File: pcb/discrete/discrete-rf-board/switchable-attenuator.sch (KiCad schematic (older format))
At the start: 11 parts, among them U1101 BGS12PL6E6327XTSA1, U1102 BGS12PL6E6327XTSA1

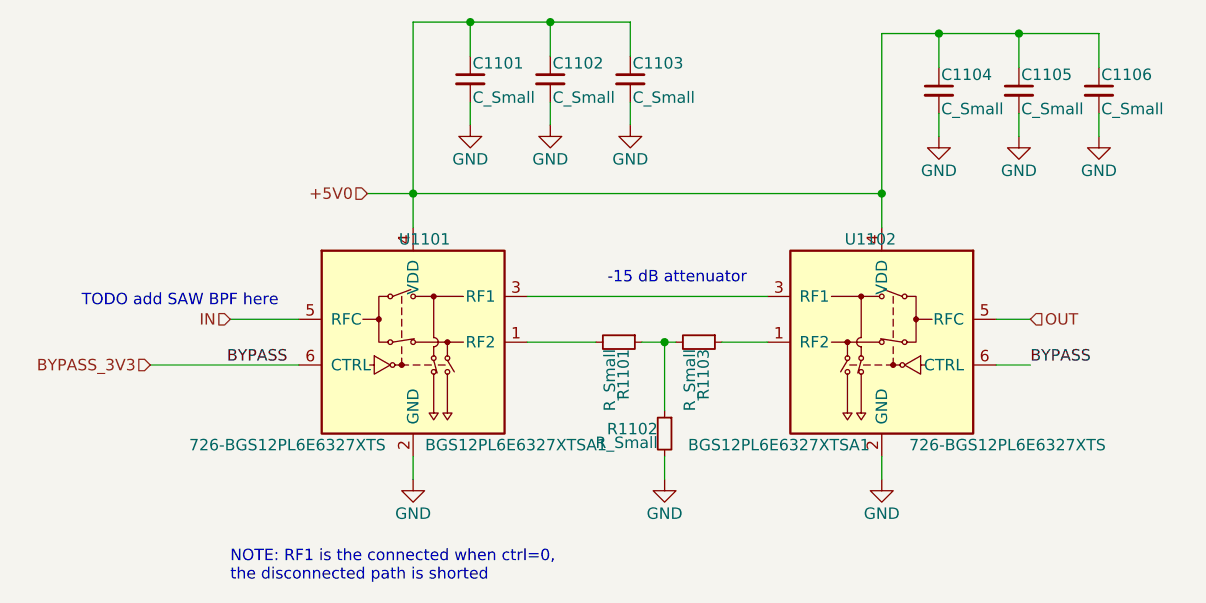
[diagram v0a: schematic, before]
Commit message: Wire out all control signals to connectors TODO PLL charge pump loop, bypass caps in attenuator circuit, antialiasing filter for ADC frontend
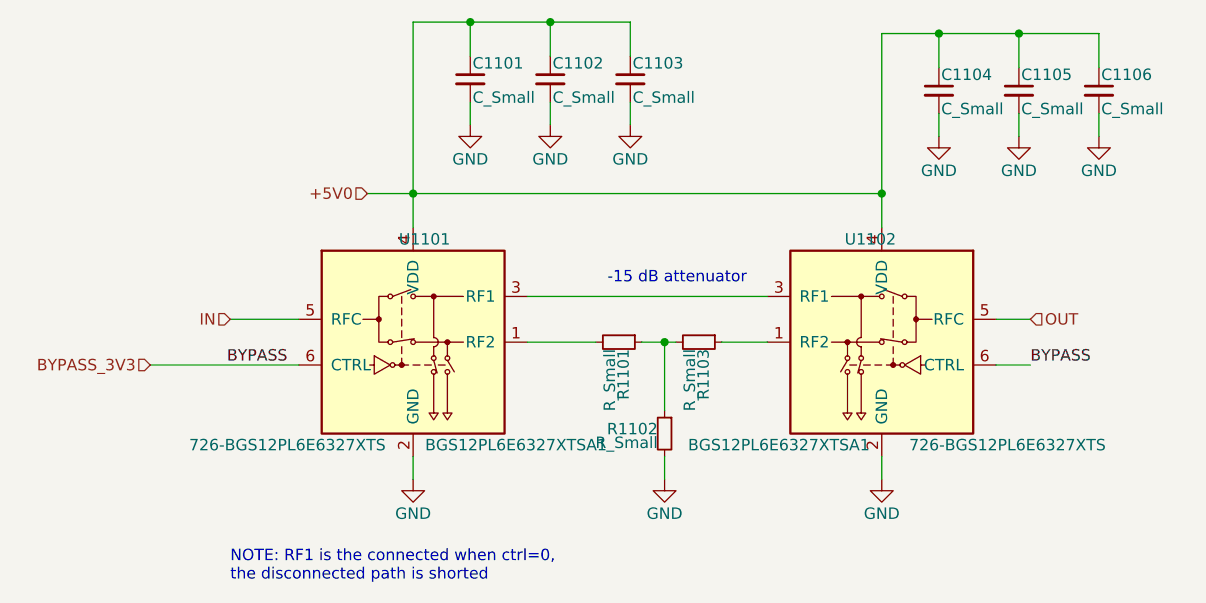
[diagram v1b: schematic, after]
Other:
- note removed: "TODO add SAW BPF here"
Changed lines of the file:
@@
 $Descr A4 11693 8268
 encoding utf-8
-Sheet 11 19
+Sheet 17 19
 Title ""
 Date ""
@@
 	1    0    0    -1
 $EndComp
-Text Notes 2500 3150 0    50   ~ 0
-TODO add SAW BPF here
 $Comp
 L Device:R_Small R?

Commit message: Start work in footprinting everything
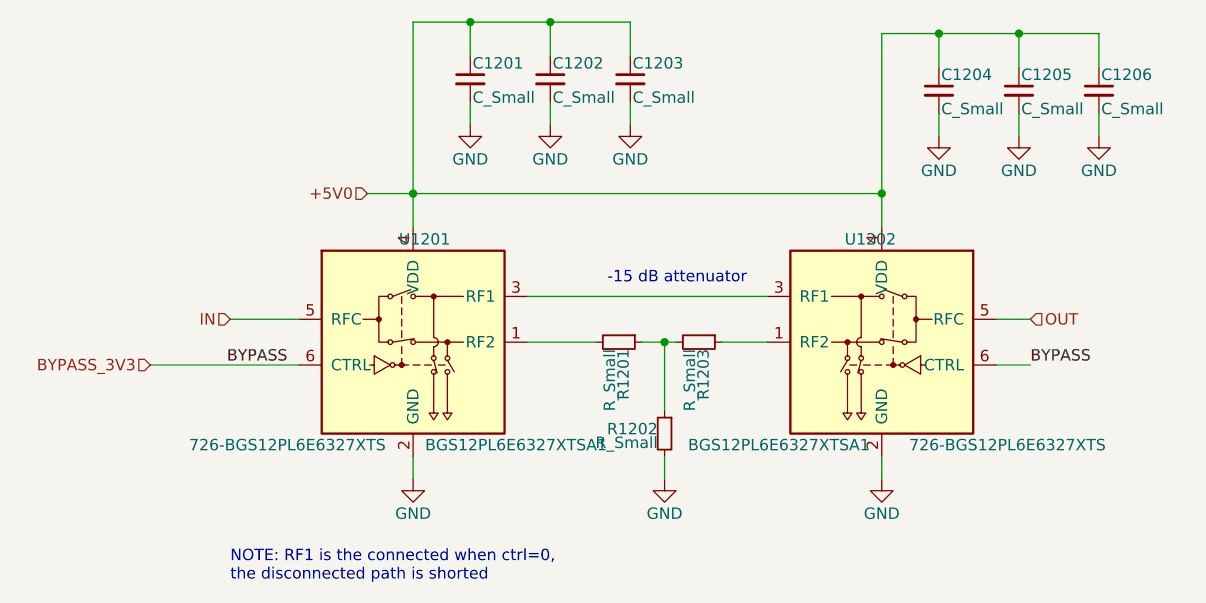
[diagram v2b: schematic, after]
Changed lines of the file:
@@
 $Descr A4 11693 8268
 encoding utf-8
-Sheet 17 19
+Sheet 18 19
 Title ""
 Date ""
@@
 AR Path="/5CA6B0AA/5CE74EBE/5D4B0AA8/5D4B1FC3" Ref="U1101"  Part="1"
 AR Path="/5CA6B0AA/5CE74EBE/5D4C7749/5D4B1FC3" Ref="U1201"  Part="1"
-F 0 "U1101" H 4000 3750 50  0000 C CNN
+F 0 "U1201" H 4000 3750 50  0000 C CNN
 F 1 "BGS12PL6E6327XTSA1" H 4400 2850 50  0000 C CNN
 F 2 "" H 3950 3300 50  0001 C CNN
@@
 AR Path="/5CA6B0AA/5CE74EBE/5D4B0AA8/5D4B1FCA" Ref="R1101"  Part="1"
 AR Path="/5CA6B0AA/5CE74EBE/5D4C7749/5D4B1FCA" Ref="R1201"  Part="1"
-F 0 "R1101" H 4880 3320 50  0000 L CNN
+F 0 "R1201" H 4880 3320 50  0000 L CNN
 F 1 "R_Small" H 4880 3260 50  0000 L CNN
 F 2 "" H 4850 3300 50  0001 C CNN
@@
 AR Path="/5CA6B0AA/5CE74EBE/5D4B0AA8/5D4B1FD0" Ref="R1103"  Part="1"
 AR Path="/5CA6B0AA/5CE74EBE/5D4C7749/5D4B1FD0" Ref="R1203"  Part="1"
-F 0 "R1103" H 5230 3320 50  0000 L CNN
+F 0 "R1203" H 5230 3320 50  0000 L CNN
 F 1 "R_Small" H 5230 3260 50  0000 L CNN
 F 2 "" H 5200 3300 50  0001 C CNN
@@
 AR Path="/5CA6B0AA/5CE74EBE/5D4B0AA8/5D4B1FD6" Ref="R1102"  Part="1"
 AR Path="/5CA6B0AA/5CE74EBE/5D4C7749/5D4B1FD6" Ref="R1202"  Part="1"
-F 0 "R1102" H 5080 3720 50  0000 L CNN
+F 0 "R1202" H 5080 3720 50  0000 L CNN
 F 1 "R_Small" H 5080 3660 50  0000 L CNN
 F 2 "" H 5050 3700 50  0001 C CNN
@@
 AR Path="/5CA6B0AA/5CE74EBE/5D4B0AA8/5D4B1FDD" Ref="#PWR01101"  Part="1"
 AR Path="/5CA6B0AA/5CE74EBE/5D4C7749/5D4B1FDD" Ref="#PWR01201"  Part="1"
-F 0 "#PWR01101" H 3950 3650 50  0001 C CNN
+F 0 "#PWR01201" H 3950 3650 50  0001 C CNN
 F 1 "GND" H 3950 3750 50  0000 C CNN
 F 2 "" H 3950 3900 50  0001 C CNN
@@
 AR Path="/5CA6B0AA/5CE74EBE/5D4B0AA8/5D4B1FE5" Ref="#PWR01105"  Part="1"
 AR Path="/5CA6B0AA/5CE74EBE/5D4C7749/5D4B1FE5" Ref="#PWR01205"  Part="1"
-F 0 "#PWR01105" H 5050 3650 50  0001 C CNN
+F 0 "#PWR01205" H 5050 3650 50  0001 C CNN
 F 1 "GND" H 5050 3750 50  0000 C CNN
 F 2 "" H 5050 3900 50  0001 C CNN
@@
 AR Path="/5CA6B0AA/5CE74EBE/5D4B0AA8/5D4B2001" Ref="#PWR01106"  Part="1"
 AR Path="/5CA6B0AA/5CE74EBE/5D4C7749/5D4B2001" Ref="#PWR01206"  Part="1"
-F 0 "#PWR01106" H 6000 3650 50  0001 C CNN
+F 0 "#PWR01206" H 6000 3650 50  0001 C CNN
 F 1 "GND" H 6000 3750 50  0000 C CNN
 F 2 "" H 6000 3900 50  0001 C CNN
@@
 AR Path="/5CA6B0AA/5CE74EBE/5D4B0AA8/5D4B1FF8" Ref="U1102"  Part="1"
 AR Path="/5CA6B0AA/5CE74EBE/5D4C7749/5D4B1FF8" Ref="U1202"  Part="1"
-F 0 "U1102" H 6050 3750 50  0000 C CNN
+F 0 "U1202" H 6050 3750 50  0000 C CNN
 F 1 "BGS12PL6E6327XTSA1" H 6450 2850 50  0000 C CNN
 F 2 "" H 6000 3300 50  0001 C CNN
@@
 AR Path="/5CA6B0AA/5CE74EBE/5D4B0AA8/5D4BC42E" Ref="C1101"  Part="1"
 AR Path="/5CA6B0AA/5CE74EBE/5D4C7749/5D4BC42E" Ref="C1201"  Part="1"
-F 0 "C1101" H 4210 2220 50  0000 L CNN
+F 0 "C1201" H 4210 2220 50  0000 L CNN
 F 1 "C_Small" H 4210 2070 50  0000 L CNN
 F 2 "" H 4200 2150 50  0001 C CNN
@@
 AR Path="/5CA6B0AA/5CE74EBE/5D4B0AA8/5D4BC853" Ref="C1102"  Part="1"
 AR Path="/5CA6B0AA/5CE74EBE/5D4C7749/5D4BC853" Ref="C1202"  Part="1"
-F 0 "C1102" H 4560 2220 50  0000 L CNN
+F 0 "C1202" H 4560 2220 50  0000 L CNN
 F 1 "C_Small" H 4560 2070 50  0000 L CNN
 F 2 "" H 4550 2150 50  0001 C CNN
@@
 AR Path="/5CA6B0AA/5CE74EBE/5D4B0AA8/5D4BCC70" Ref="C1103"  Part="1"
 AR Path="/5CA6B0AA/5CE74EBE/5D4C7749/5D4BCC70" Ref="C1203"  Part="1"
-F 0 "C1103" H 4910 2220 50  0000 L CNN
+F 0 "C1203" H 4910 2220 50  0000 L CNN
 F 1 "C_Small" H 4910 2070 50  0000 L CNN
 F 2 "" H 4900 2150 50  0001 C CNN
@@
 AR Path="/5CA6B0AA/5CE74EBE/5D4B0AA8/5D4BED00" Ref="C1104"  Part="1"
 AR Path="/5CA6B0AA/5CE74EBE/5D4C7749/5D4BED00" Ref="C1204"  Part="1"
-F 0 "C1104" H 6260 2270 50  0000 L CNN
+F 0 "C1204" H 6260 2270 50  0000 L CNN
 F 1 "C_Small" H 6260 2120 50  0000 L CNN
 F 2 "" H 6250 2200 50  0001 C CNN
@@
 AR Path="/5CA6B0AA/5CE74EBE/5D4B0AA8/5D4BED06" Ref="C1105"  Part="1"
 AR Path="/5CA6B0AA/5CE74EBE/5D4C7749/5D4BED06" Ref="C1205"  Part="1"
-F 0 "C1105" H 6610 2270 50  0000 L CNN
+F 0 "C1205" H 6610 2270 50  0000 L CNN
 F 1 "C_Small" H 6610 2120 50  0000 L CNN
 F 2 "" H 6600 2200 50  0001 C CNN
@@
 AR Path="/5CA6B0AA/5CE74EBE/5D4B0AA8/5D4BED0C" Ref="C1106"  Part="1"
 AR Path="/5CA6B0AA/5CE74EBE/5D4C7749/5D4BED0C" Ref="C1206"  Part="1"
-F 0 "C1106" H 6960 2270 50  0000 L CNN
+F 0 "C1206" H 6960 2270 50  0000 L CNN
 F 1 "C_Small" H 6960 2120 50  0000 L CNN
 F 2 "" H 6950 2200 50  0001 C CNN
@@
 AR Path="/5CA6B0AA/5CE74EBE/5D4B0AA8/5D4BF277" Ref="#PWR01109"  Part="1"
 AR Path="/5CA6B0AA/5CE74EBE/5D4C7749/5D4BF277" Ref="#PWR01209"  Part="1"
-F 0 "#PWR01109" H 6950 2150 50  0001 C CNN
+F 0 "#PWR01209" H 6950 2150 50  0001 C CNN
 F 1 "GND" H 6950 2250 50  0000 C CNN
 F 2 "" H 6950 2400 50  0001 C CNN
@@
 AR Path="/5CA6B0AA/5CE74EBE/5D4B0AA8/5D4BF7E8" Ref="#PWR01108"  Part="1"
 AR Path="/5CA6B0AA/5CE74EBE/5D4C7749/5D4BF7E8" Ref="#PWR01208"  Part="1"
-F 0 "#PWR01108" H 6600 2150 50  0001 C CNN
+F 0 "#PWR01208" H 6600 2150 50  0001 C CNN
 F 1 "GND" H 6600 2250 50  0000 C CNN
 F 2 "" H 6600 2400 50  0001 C CNN
@@
 AR Path="/5CA6B0AA/5CE74EBE/5D4B0AA8/5D4BFA67" Ref="#PWR01107"  Part="1"
 AR Path="/5CA6B0AA/5CE74EBE/5D4C7749/5D4BFA67" Ref="#PWR01207"  Part="1"
-F 0 "#PWR01107" H 6250 2150 50  0001 C CNN
+F 0 "#PWR01207" H 6250 2150 50  0001 C CNN
 F 1 "GND" H 6250 2250 50  0000 C CNN
 F 2 "" H 6250 2400 50  0001 C CNN
@@
 AR Path="/5CA6B0AA/5CE74EBE/5D4B0AA8/5D4C425B" Ref="#PWR01104"  Part="1"
 AR Path="/5CA6B0AA/5CE74EBE/5D4C7749/5D4C425B" Ref="#PWR01204"  Part="1"
-F 0 "#PWR01104" H 4900 2100 50  0001 C CNN
+F 0 "#PWR01204" H 4900 2100 50  0001 C CNN
 F 1 "GND" H 4900 2200 50  0000 C CNN
 F 2 "" H 4900 2350 50  0001 C CNN
@@
 AR Path="/5CA6B0AA/5CE74EBE/5D4B0AA8/5D4C4261" Ref="#PWR01103"  Part="1"
 AR Path="/5CA6B0AA/5CE74EBE/5D4C7749/5D4C4261" Ref="#PWR01203"  Part="1"
-F 0 "#PWR01103" H 4550 2100 50  0001 C CNN
+F 0 "#PWR01203" H 4550 2100 50  0001 C CNN
 F 1 "GND" H 4550 2200 50  0000 C CNN
 F 2 "" H 4550 2350 50  0001 C CNN
@@
 AR Path="/5CA6B0AA/5CE74EBE/5D4B0AA8/5D4C4267" Ref="#PWR01102"  Part="1"
 AR Path="/5CA6B0AA/5CE74EBE/5D4C7749/5D4C4267" Ref="#PWR01202"  Part="1"
-F 0 "#PWR01102" H 4200 2100 50  0001 C CNN
+F 0 "#PWR01202" H 4200 2100 50  0001 C CNN
 F 1 "GND" H 4200 2200 50  0000 C CNN
 F 2 "" H 4200 2350 50  0001 C CNN

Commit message: Fix some parts
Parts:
- U1101: footprint (none) -> discrete_footprints:Infineon_TSLP-6-4
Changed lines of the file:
@@
 $Descr A4 11693 8268
 encoding utf-8
-Sheet 18 19
+Sheet 17 19
 Title ""
 Date ""
@@
 AR Path="/5CA6B0AA/5CE74EBE/5D4B0AA8/5D4B1FC3" Ref="U1101"  Part="1"
 AR Path="/5CA6B0AA/5CE74EBE/5D4C7749/5D4B1FC3" Ref="U1201"  Part="1"
-F 0 "U1201" H 4000 3750 50  0000 C CNN
+F 0 "U1101" H 4000 3750 50  0000 C CNN
 F 1 "BGS12PL6E6327XTSA1" H 4400 2850 50  0000 C CNN
-F 2 "" H 3950 3300 50  0001 C CNN
+F 2 "discrete_footprints:Infineon_TSLP-6-4" H 3950 3300 50  0001 C CNN
 F 3 "" H 3950 3300 50  0001 C CNN
 F 4 "726-BGS12PL6E6327XTS" H 3400 2850 50  0000 C CNN "Mouser"
@@
 AR Path="/5CA6B0AA/5CE74EBE/5D4B0AA8/5D4B1FCA" Ref="R1101"  Part="1"
 AR Path="/5CA6B0AA/5CE74EBE/5D4C7749/5D4B1FCA" Ref="R1201"  Part="1"
-F 0 "R1201" H 4880 3320 50  0000 L CNN
+F 0 "R1101" H 4880 3320 50  0000 L CNN
 F 1 "R_Small" H 4880 3260 50  0000 L CNN
 F 2 "" H 4850 3300 50  0001 C CNN
@@
 AR Path="/5CA6B0AA/5CE74EBE/5D4B0AA8/5D4B1FD0" Ref="R1103"  Part="1"
 AR Path="/5CA6B0AA/5CE74EBE/5D4C7749/5D4B1FD0" Ref="R1203"  Part="1"
-F 0 "R1203" H 5230 3320 50  0000 L CNN
+F 0 "R1103" H 5230 3320 50  0000 L CNN
 F 1 "R_Small" H 5230 3260 50  0000 L CNN
 F 2 "" H 5200 3300 50  0001 C CNN
@@
 AR Path="/5CA6B0AA/5CE74EBE/5D4B0AA8/5D4B1FD6" Ref="R1102"  Part="1"
 AR Path="/5CA6B0AA/5CE74EBE/5D4C7749/5D4B1FD6" Ref="R1202"  Part="1"
-F 0 "R1202" H 5080 3720 50  0000 L CNN
+F 0 "R1102" H 5080 3720 50  0000 L CNN
 F 1 "R_Small" H 5080 3660 50  0000 L CNN
 F 2 "" H 5050 3700 50  0001 C CNN
@@
 AR Path="/5CA6B0AA/5CE74EBE/5D4B0AA8/5D4B1FDD" Ref="#PWR01101"  Part="1"
 AR Path="/5CA6B0AA/5CE74EBE/5D4C7749/5D4B1FDD" Ref="#PWR01201"  Part="1"
-F 0 "#PWR01201" H 3950 3650 50  0001 C CNN
+F 0 "#PWR01101" H 3950 3650 50  0001 C CNN
 F 1 "GND" H 3950 3750 50  0000 C CNN
 F 2 "" H 3950 3900 50  0001 C CNN
@@
 AR Path="/5CA6B0AA/5CE74EBE/5D4B0AA8/5D4B1FE5" Ref="#PWR01105"  Part="1"
 AR Path="/5CA6B0AA/5CE74EBE/5D4C7749/5D4B1FE5" Ref="#PWR01205"  Part="1"
-F 0 "#PWR01205" H 5050 3650 50  0001 C CNN
+F 0 "#PWR01105" H 5050 3650 50  0001 C CNN
 F 1 "GND" H 5050 3750 50  0000 C CNN
 F 2 "" H 5050 3900 50  0001 C CNN
@@
 AR Path="/5CA6B0AA/5CE74EBE/5D4B0AA8/5D4B2001" Ref="#PWR01106"  Part="1"
 AR Path="/5CA6B0AA/5CE74EBE/5D4C7749/5D4B2001" Ref="#PWR01206"  Part="1"
-F 0 "#PWR01206" H 6000 3650 50  0001 C CNN
+F 0 "#PWR01106" H 6000 3650 50  0001 C CNN
 F 1 "GND" H 6000 3750 50  0000 C CNN
 F 2 "" H 6000 3900 50  0001 C CNN
@@
 AR Path="/5CA6B0AA/5CE74EBE/5D4B0AA8/5D4B1FF8" Ref="U1102"  Part="1"
 AR Path="/5CA6B0AA/5CE74EBE/5D4C7749/5D4B1FF8" Ref="U1202"  Part="1"
-F 0 "U1202" H 6050 3750 50  0000 C CNN
+F 0 "U1102" H 6050 3750 50  0000 C CNN
 F 1 "BGS12PL6E6327XTSA1" H 6450 2850 50  0000 C CNN
 F 2 "" H 6000 3300 50  0001 C CNN
@@
 AR Path="/5CA6B0AA/5CE74EBE/5D4B0AA8/5D4BC42E" Ref="C1101"  Part="1"
 AR Path="/5CA6B0AA/5CE74EBE/5D4C7749/5D4BC42E" Ref="C1201"  Part="1"
-F 0 "C1201" H 4210 2220 50  0000 L CNN
+F 0 "C1101" H 4210 2220 50  0000 L CNN
 F 1 "C_Small" H 4210 2070 50  0000 L CNN
 F 2 "" H 4200 2150 50  0001 C CNN
@@
 AR Path="/5CA6B0AA/5CE74EBE/5D4B0AA8/5D4BC853" Ref="C1102"  Part="1"
 AR Path="/5CA6B0AA/5CE74EBE/5D4C7749/5D4BC853" Ref="C1202"  Part="1"
-F 0 "C1202" H 4560 2220 50  0000 L CNN
+F 0 "C1102" H 4560 2220 50  0000 L CNN
 F 1 "C_Small" H 4560 2070 50  0000 L CNN
 F 2 "" H 4550 2150 50  0001 C CNN
@@
 AR Path="/5CA6B0AA/5CE74EBE/5D4B0AA8/5D4BCC70" Ref="C1103"  Part="1"
 AR Path="/5CA6B0AA/5CE74EBE/5D4C7749/5D4BCC70" Ref="C1203"  Part="1"
-F 0 "C1203" H 4910 2220 50  0000 L CNN
+F 0 "C1103" H 4910 2220 50  0000 L CNN
 F 1 "C_Small" H 4910 2070 50  0000 L CNN
 F 2 "" H 4900 2150 50  0001 C CNN
@@
 AR Path="/5CA6B0AA/5CE74EBE/5D4B0AA8/5D4BED00" Ref="C1104"  Part="1"
 AR Path="/5CA6B0AA/5CE74EBE/5D4C7749/5D4BED00" Ref="C1204"  Part="1"
-F 0 "C1204" H 6260 2270 50  0000 L CNN
+F 0 "C1104" H 6260 2270 50  0000 L CNN
 F 1 "C_Small" H 6260 2120 50  0000 L CNN
 F 2 "" H 6250 2200 50  0001 C CNN
@@
 AR Path="/5CA6B0AA/5CE74EBE/5D4B0AA8/5D4BED06" Ref="C1105"  Part="1"
 AR Path="/5CA6B0AA/5CE74EBE/5D4C7749/5D4BED06" Ref="C1205"  Part="1"
-F 0 "C1205" H 6610 2270 50  0000 L CNN
+F 0 "C1105" H 6610 2270 50  0000 L CNN
 F 1 "C_Small" H 6610 2120 50  0000 L CNN
 F 2 "" H 6600 2200 50  0001 C CNN
@@
 AR Path="/5CA6B0AA/5CE74EBE/5D4B0AA8/5D4BED0C" Ref="C1106"  Part="1"
 AR Path="/5CA6B0AA/5CE74EBE/5D4C7749/5D4BED0C" Ref="C1206"  Part="1"
-F 0 "C1206" H 6960 2270 50  0000 L CNN
+F 0 "C1106" H 6960 2270 50  0000 L CNN
 F 1 "C_Small" H 6960 2120 50  0000 L CNN
 F 2 "" H 6950 2200 50  0001 C CNN
@@
 AR Path="/5CA6B0AA/5CE74EBE/5D4B0AA8/5D4BF277" Ref="#PWR01109"  Part="1"
 AR Path="/5CA6B0AA/5CE74EBE/5D4C7749/5D4BF277" Ref="#PWR01209"  Part="1"
-F 0 "#PWR01209" H 6950 2150 50  0001 C CNN
+F 0 "#PWR01109" H 6950 2150 50  0001 C CNN
 F 1 "GND" H 6950 2250 50  0000 C CNN
 F 2 "" H 6950 2400 50  0001 C CNN
@@
 AR Path="/5CA6B0AA/5CE74EBE/5D4B0AA8/5D4BF7E8" Ref="#PWR01108"  Part="1"
 AR Path="/5CA6B0AA/5CE74EBE/5D4C7749/5D4BF7E8" Ref="#PWR01208"  Part="1"
-F 0 "#PWR01208" H 6600 2150 50  0001 C CNN
+F 0 "#PWR01108" H 6600 2150 50  0001 C CNN
 F 1 "GND" H 6600 2250 50  0000 C CNN
 F 2 "" H 6600 2400 50  0001 C CNN
@@
 AR Path="/5CA6B0AA/5CE74EBE/5D4B0AA8/5D4BFA67" Ref="#PWR01107"  Part="1"
 AR Path="/5CA6B0AA/5CE74EBE/5D4C7749/5D4BFA67" Ref="#PWR01207"  Part="1"
-F 0 "#PWR01207" H 6250 2150 50  0001 C CNN
+F 0 "#PWR01107" H 6250 2150 50  0001 C CNN
 F 1 "GND" H 6250 2250 50  0000 C CNN
 F 2 "" H 6250 2400 50  0001 C CNN
@@
 AR Path="/5CA6B0AA/5CE74EBE/5D4B0AA8/5D4C425B" Ref="#PWR01104"  Part="1"
 AR Path="/5CA6B0AA/5CE74EBE/5D4C7749/5D4C425B" Ref="#PWR01204"  Part="1"
-F 0 "#PWR01204" H 4900 2100 50  0001 C CNN
+F 0 "#PWR01104" H 4900 2100 50  0001 C CNN
 F 1 "GND" H 4900 2200 50  0000 C CNN
 F 2 "" H 4900 2350 50  0001 C CNN
@@
 AR Path="/5CA6B0AA/5CE74EBE/5D4B0AA8/5D4C4261" Ref="#PWR01103"  Part="1"
 AR Path="/5CA6B0AA/5CE74EBE/5D4C7749/5D4C4261" Ref="#PWR01203"  Part="1"
-F 0 "#PWR01203" H 4550 2100 50  0001 C CNN
+F 0 "#PWR01103" H 4550 2100 50  0001 C CNN
 F 1 "GND" H 4550 2200 50  0000 C CNN
 F 2 "" H 4550 2350 50  0001 C CNN
@@
 AR Path="/5CA6B0AA/5CE74EBE/5D4B0AA8/5D4C4267" Ref="#PWR01102"  Part="1"
 AR Path="/5CA6B0AA/5CE74EBE/5D4C7749/5D4C4267" Ref="#PWR01202"  Part="1"
-F 0 "#PWR01202" H 4200 2100 50  0001 C CNN
+F 0 "#PWR01102" H 4200 2100 50  0001 C CNN
 F 1 "GND" H 4200 2200 50  0000 C CNN
 F 2 "" H 4200 2350 50  0001 C CNN

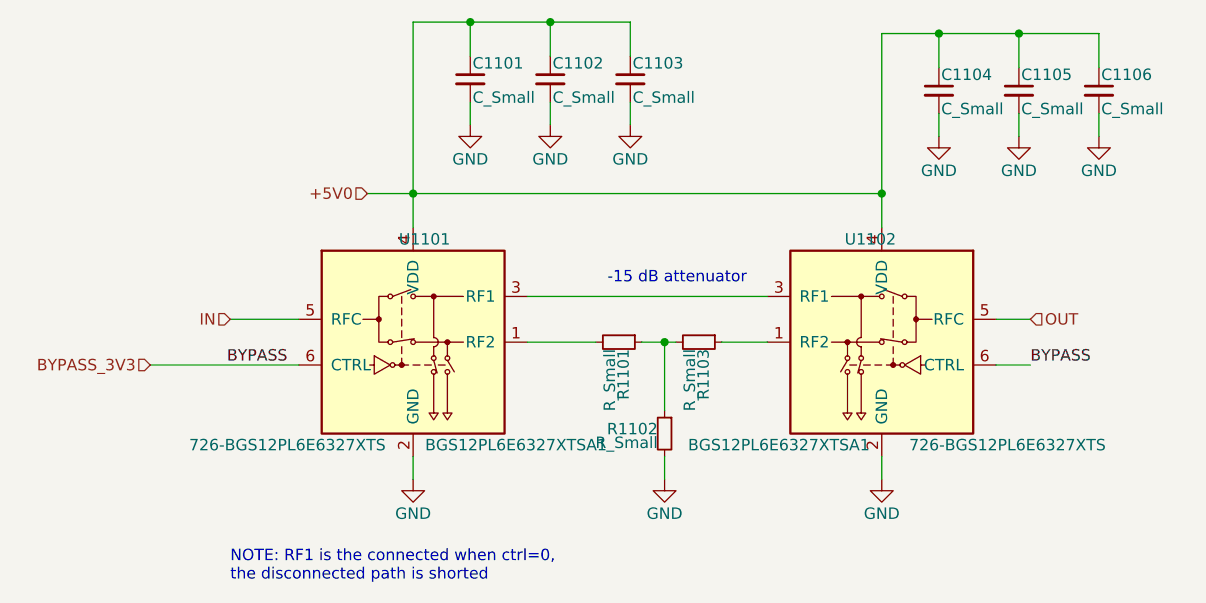
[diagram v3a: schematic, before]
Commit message: Add matching PNP/NPN transistor pairs, fix pin numbering for BFU520R transistors TODO fix biasing on power stage, source last NPN transistor, autofill and start sourcing passives
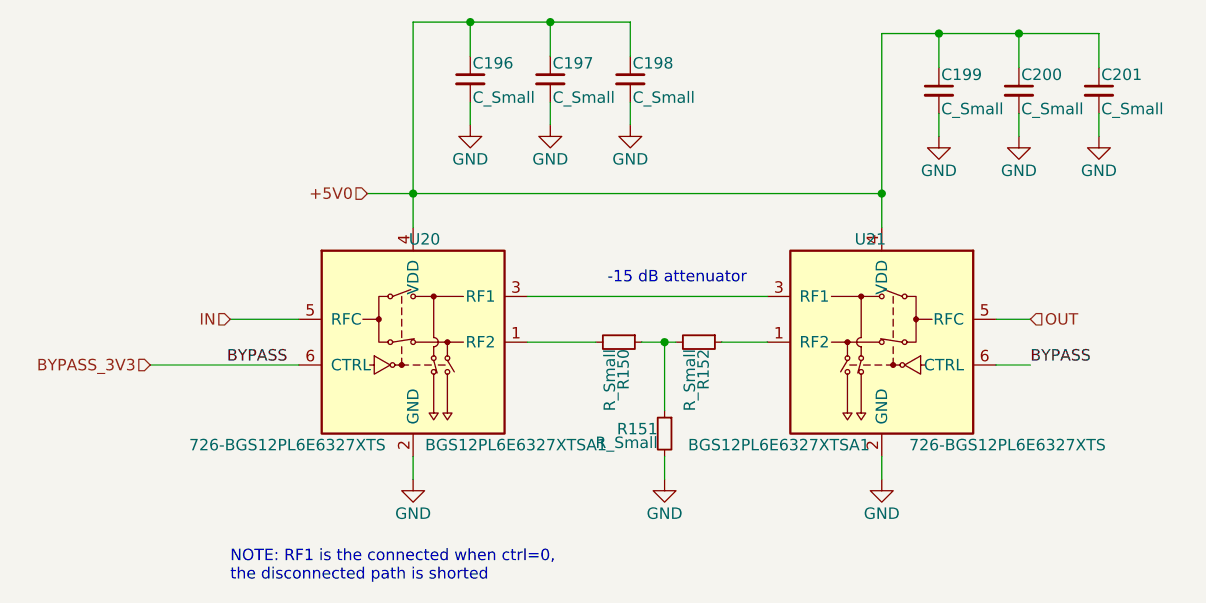
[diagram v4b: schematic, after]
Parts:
- renumbered C1101 to C190, C1102 to C191, C1103 to C192, C1104 to C193, C1105 to C194, C1106 to C195, R1101 to R147, R1102 to R148, R1103 to R149, U1101 to U18, U1102 to U19
